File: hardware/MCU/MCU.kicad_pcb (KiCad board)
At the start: 2 copper layers, 40 x 40 mm, 39 parts, among them P1 CONN_01X05, P2 CONN_01X04, P3 CONN_01X05, U1 MAX6369, U2 DS18B20, U3 TC1262-30VDB, U4 PIC18F45K22, U5 LTC6082, Y1 Crystal

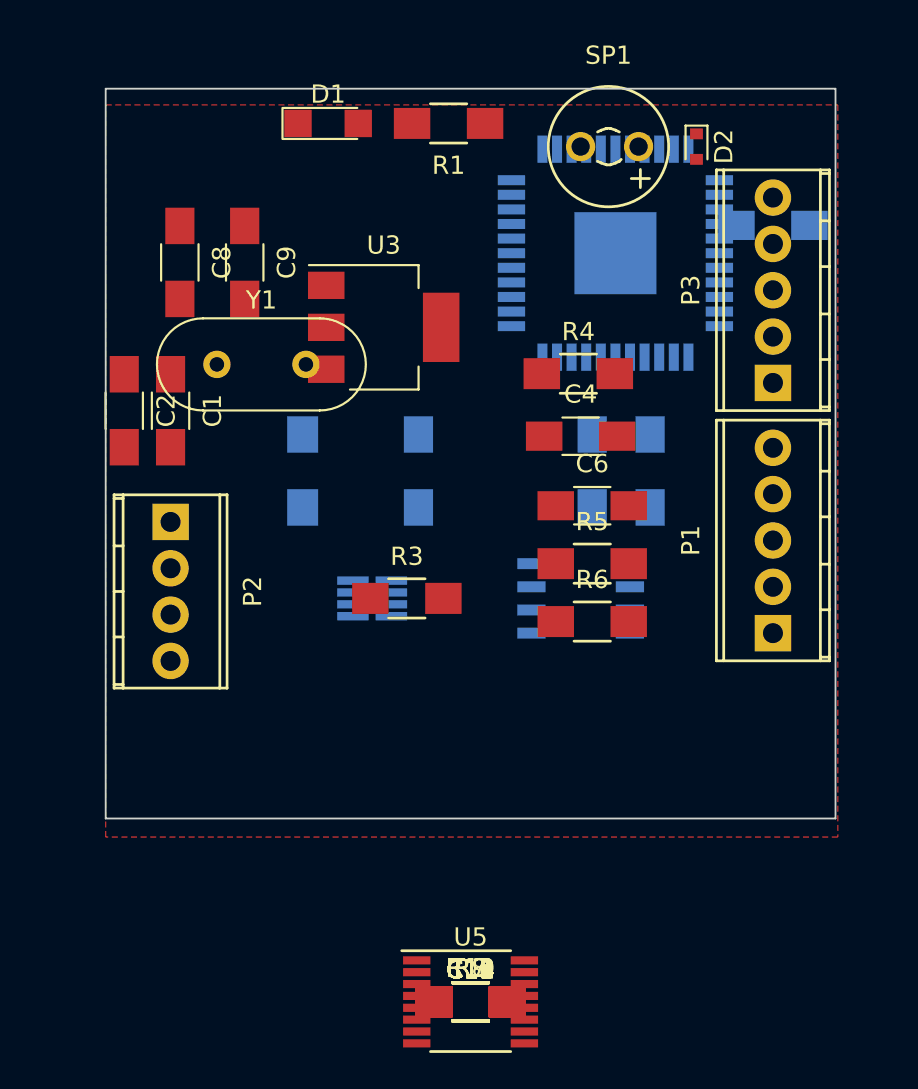
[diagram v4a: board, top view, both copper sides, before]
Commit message: Puestas todas las huellas. Primera colocacion de los componentes hecha. A la espera de la revision de los esquematicos para rutar
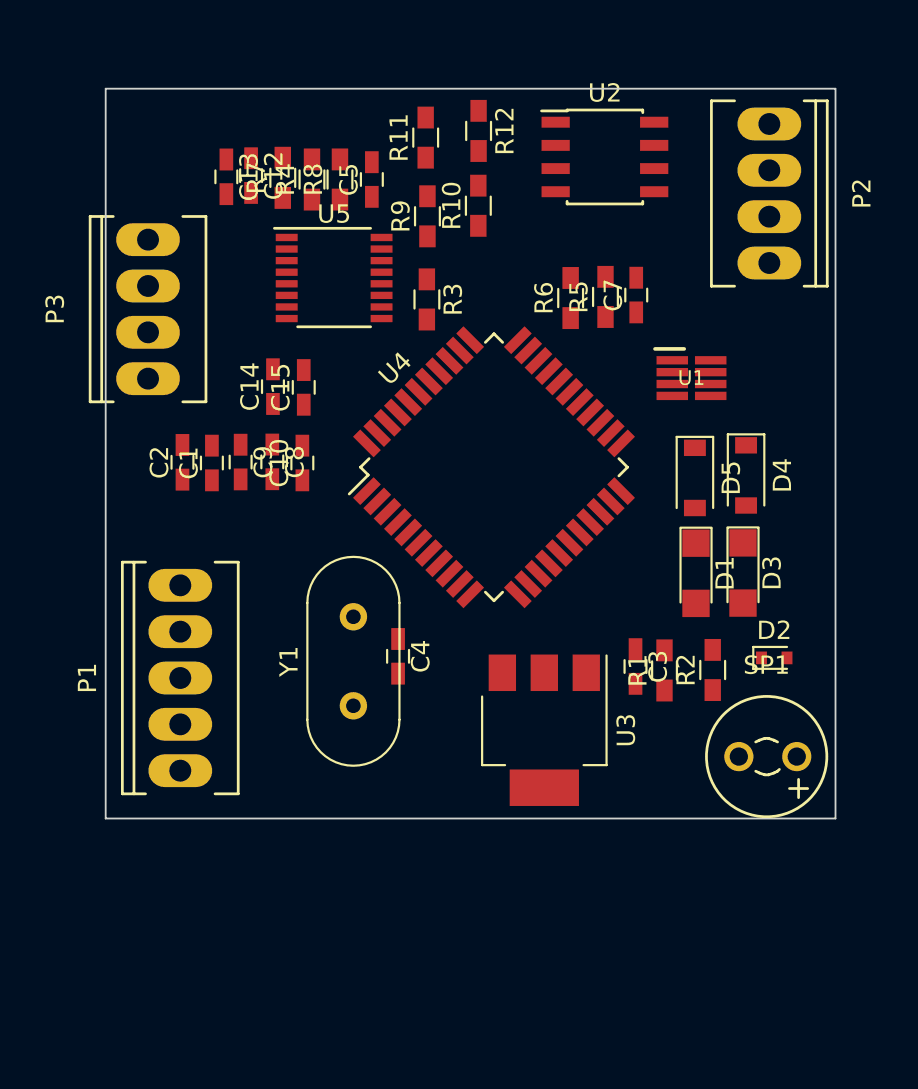
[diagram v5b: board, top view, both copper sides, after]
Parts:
- removed C11, C6: 100nF, Capacitors_SMD:C_1206_HandSoldering
- added D3: LED, LEDs:LED_1206, F.Cu at (47.0, 184.7)
- added D4: ZENER, Diodes_SMD:D_SOD-123, F.Cu at (47.2, 179.3)
- added D5: ZENER, Diodes_SMD:D_SOD-123, F.Cu at (44.4, 179.5)
- C1, C12, C13, C14, C15, C2, C4, C8, C9: footprint Capacitors_SMD:C_1206_HandSoldering -> Capacitors_SMD:C_0603_HandSoldering
- C10, C3, C5, C7: footprint Capacitors_SMD:C_1206_HandSoldering -> Capacitors_SMD:C_0603_HandSoldering; moved to F.Cu
- P1: footprint Connectors_Terminal_Blocks:TerminalBlock_Pheonix_MPT-2.54mm_5pol -> Sockets_MOLEX_KK-System:Socket_MOLEX-KK-RM2-54mm_Lock_5pin_straight
- P2: footprint Connectors_Terminal_Blocks:TerminalBlock_Pheonix_MPT-2.54mm_4pol -> Sockets_MOLEX_KK-System:Socket_MOLEX-KK-RM2-54mm_Lock_4pin_straight
- P3: footprint Connectors_Terminal_Blocks:TerminalBlock_Pheonix_MPT-2.54mm_5pol -> Sockets_MOLEX_KK-System:Socket_MOLEX-KK-RM2-54mm_Lock_4pin_straight
- R1, R10, R11, R12, R3, R4, R5, R6, R7, R8, R9: footprint Resistors_SMD:R_1206_HandSoldering -> Resistors_SMD:R_0603_HandSoldering
- R2: footprint Resistors_SMD:R_1206_HandSoldering -> Resistors_SMD:R_0603_HandSoldering; moved to F.Cu
- U1, U2: moved to F.Cu
- U4: footprint Housings_QFP:TQFP-44-1EP_10x10mm_Pitch0.8mm -> Housings_QFP:LQFP-44_10x10mm_Pitch0.8mm; moved to F.Cu
- U5: value LTC6082 -> LT6005; footprint Housings_SSOP:TSSOP-16_4.4x5mm_Pitch0.65mm -> Housings_SSOP:SSOP-16_3.9x4.9mm_Pitch0.635mm
- moved R12 47.7 mm to (32.5, 160.4), turned to 270 degrees
- moved R11 47.4 mm to (29.6, 160.8), turned to 90 degrees
- moved C13 47.2 mm to (18.7, 162.9), turned to 270 degrees
- moved C12 46.9 mm to (20.0, 162.9), turned to 270 degrees
- moved R7 46.3 mm to (21.8, 163.0), turned to 90 degrees
- moved R8 45.6 mm to (24.9, 163.1), turned to 90 degrees
- moved R10 43.6 mm to (32.5, 164.5), turned to 90 degrees
- moved R9 43.1 mm to (29.7, 165.1), turned to 90 degrees
- moved U5 40.4 mm to (24.6, 168.5)
- moved P2 37.4 mm to (48.4, 163.9)
- moved C14 35.4 mm to (21.2, 174.4), turned to 90 degrees
- moved C15 34.9 mm to (22.9, 174.5), turned to 90 degrees
- moved SP1 34.5 mm to (46.8, 194.7)
- moved P3 34.5 mm to (14.4, 170.2)
- moved P1 32.6 mm to (16.2, 190.4)
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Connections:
- C12 pad 1: Net-(C11-Pad1) -> VCC
- C12 pad 2: GND -> Net-(C12-Pad2)
- C13 pad 1: Net-(C11-Pad1) -> VCC
- C13 pad 2: GND -> Net-(C12-Pad2)
- R2 pad 2: (no net) -> Net-(D3-Pad2)
- U5 pad 12: /RF_IN -> (no net)
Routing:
- removed copper zone on F.Cu, net GND

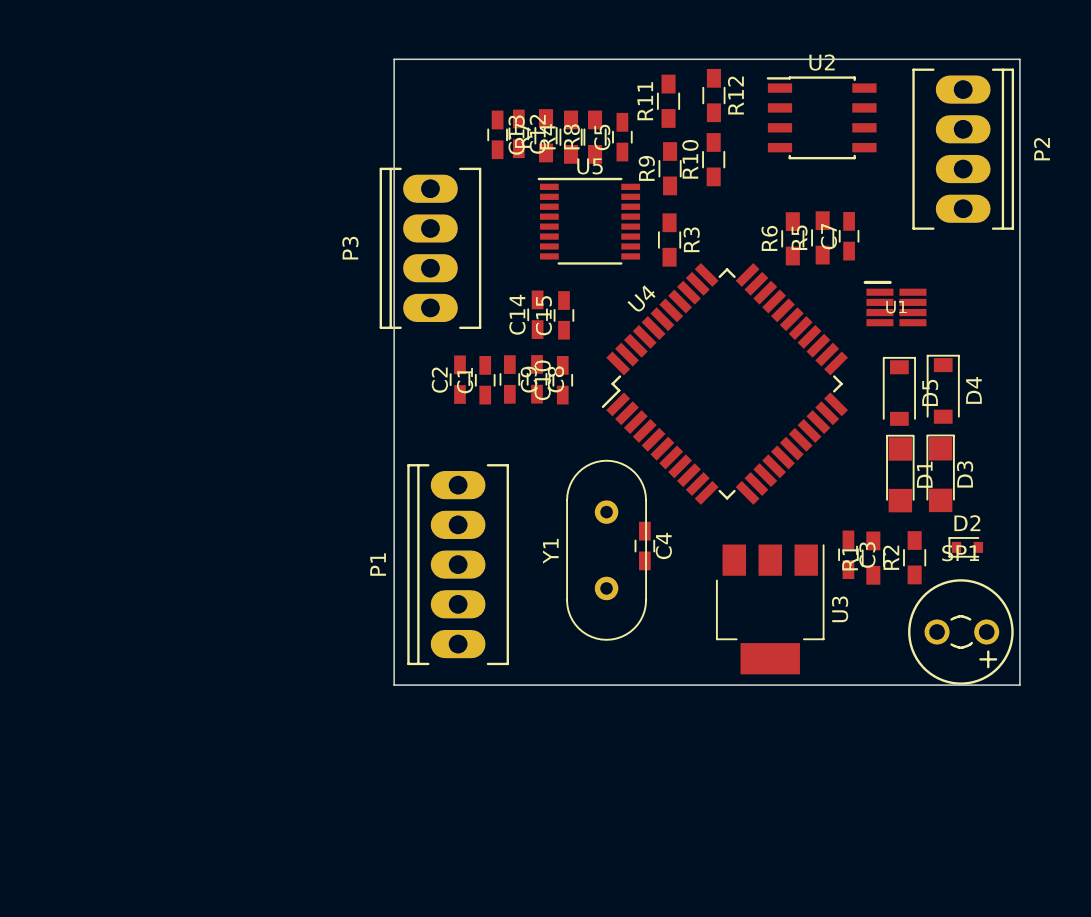
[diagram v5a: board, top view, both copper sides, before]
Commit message: Añadidas señales PTT, RPT, HIPWR, BEACON_MODE. Añadido un conector
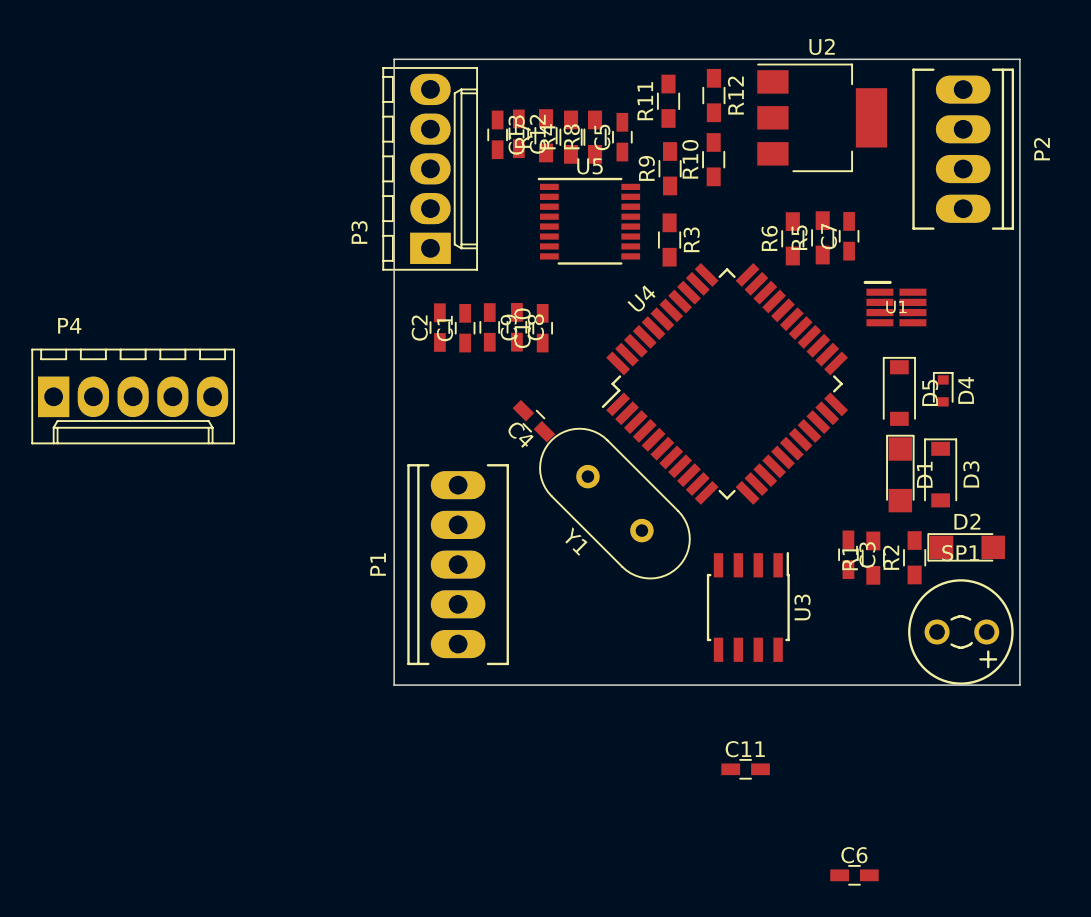
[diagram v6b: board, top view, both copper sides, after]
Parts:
- removed C14, C15: 10nF, Capacitors_SMD:C_0603_HandSoldering
- added C11: 100nF, Capacitors_SMD:C_0603_HandSoldering, F.Cu at (34.5, 203.5)
- added C6: 10nF, Capacitors_SMD:C_0603_HandSoldering, F.Cu at (41.5, 210.3)
- added P4: CONN_01X05, Connectors_Molex:Molex_KK-6410-05_05x2.54mm_Straight, F.Cu at (-9.70, 179.7)
- C1: value 18pF -> C
- C12, C13: value 100nF -> 10nF
- C4: value 1uF -> 18pF
- C5: value 10nF -> 1uF
- C7: value C -> 100nF
- D2: value D -> LED; footprint Diodes_SMD:D_SOD-523 -> LEDs:LED_1206
- D3: value LED -> ZENER; footprint LEDs:LED_1206 -> Diodes_SMD:D_SOD-123
- D4: value ZENER -> D; footprint Diodes_SMD:D_SOD-123 -> Diodes_SMD:D_SOD-523
- P3: footprint Sockets_MOLEX_KK-System:Socket_MOLEX-KK-RM2-54mm_Lock_4pin_straight -> Connectors_Molex:Molex_KK-6410-05_05x2.54mm_Straight
- U2: value DS18B20 -> TC1262-30VDB; footprint Housings_SOIC:SOIC-8_3.9x4.9mm_Pitch1.27mm -> SOT-223
- U3: value TC1262-30VDB -> DS18B20; footprint SOT-223 -> Housings_SOIC:SOIC-8_3.9x4.9mm_Pitch1.27mm
- moved C4 10.7 mm to (21.0, 181.2), turned to 135 degrees
- moved Y1 4.33 mm to (27.9, 188.2), turned to 135 degrees
- moved C9 3.57 mm to (18.2, 175.3)
- moved C2 3.57 mm to (15.0, 175.3)
- moved C10 3.57 mm to (21.6, 175.3)
- moved C8 3.57 mm to (19.9, 175.2)
- moved C1 3.57 mm to (16.6, 175.3)
- moved U3 1.41 mm to (34.7, 193.2)
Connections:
- net /BEA renamed /BEACON_ON
- net /RA0 renamed /VBAT
- C1 pad 1: /RA6 -> VCC
- C10 pad 1: /DIS -> VCC
- C10 pad 2: GND -> Net-(C10-Pad2)
- C12 pad 1: VCC -> Net-(C12-Pad1)
- C12 pad 2: Net-(C12-Pad2) -> GND
- C13 pad 1: VCC -> Net-(C13-Pad1)
- C13 pad 2: Net-(C12-Pad2) -> Net-(C13-Pad2)
- C2 pad 1: /RA7 -> /RA6
- C4 pad 1: VCC -> /RA7
- C5 pad 1: Net-(C5-Pad1) -> VCC
- C7 pad 1: VCC -> /DIS
- D2 pad 1: /BUZZER -> GND
- D2 pad 2: GND -> Net-(D2-Pad2)
- D3 pad 1: GND -> /SOL
- D3 pad 2: Net-(D3-Pad2) -> GND
- D4 pad 1: /SOL -> /BUZZER
- R1 pad 1: /LED_R -> /LED_G
- R2 pad 1: /LED_G -> /LED_R
- R2 pad 2: Net-(D3-Pad2) -> Net-(D2-Pad2)
- R4 pad 1: Net-(C5-Pad1) -> Net-(C6-Pad1)
- R7 pad 2: Net-(C15-Pad2) -> Net-(C13-Pad2)
- R8 pad 1: Net-(C15-Pad2) -> Net-(C13-Pad2)
- R8 pad 2: Net-(C14-Pad1) -> Net-(C12-Pad1)
- U1 pad 3: (no net) -> Net-(U1-Pad3)
- U2 pad 1: (no net) -> VDD
- U2 pad 2: (no net) -> GND
- U2 pad 3: (no net) -> VCC
- U2 pad 4: /TEMP -> GND
- U3 pad 1: VDD -> Net-(U3-Pad1)
- U3 pad 2: GND -> Net-(U3-Pad2)
- U3 pad 3: VCC -> Net-(U3-Pad3)
- U3 pad 4: GND -> /TEMP
- U4 pad 1: (no net) -> Net-(U4-Pad1)
- U4 pad 10: (no net) -> /RPT
- U4 pad 11: (no net) -> /HIPWR
- U4 pad 12: (no net) -> Net-(U4-Pad12)
- U4 pad 13: (no net) -> Net-(U4-Pad13)
- U4 pad 14: (no net) -> /BEACON_MODE
- U4 pad 15: (no net) -> Net-(U4-Pad15)
- U4 pad 23: (no net) -> Net-(U4-Pad23)
- U4 pad 25: (no net) -> Net-(U4-Pad25)
- U4 pad 32: (no net) -> Net-(U4-Pad32)
- U4 pad 33: (no net) -> Net-(U4-Pad33)
- U4 pad 34: (no net) -> Net-(U4-Pad34)
- U4 pad 35: (no net) -> Net-(U4-Pad35)
- U4 pad 36: (no net) -> Net-(U4-Pad36)
- U4 pad 37: (no net) -> Net-(U4-Pad37)
- U4 pad 38: (no net) -> Net-(U4-Pad38)
- U4 pad 4: (no net) -> Net-(U4-Pad4)
- U4 pad 42: (no net) -> Net-(U4-Pad42)
- U4 pad 43: (no net) -> Net-(U4-Pad43)
- U4 pad 44: (no net) -> Net-(U4-Pad44)
- U4 pad 5: (no net) -> Net-(U4-Pad5)
- U4 pad 9: (no net) -> /PTT
- U5 pad 12: (no net) -> /RF_IN
- U5 pad 3: Net-(C5-Pad1) -> Net-(C6-Pad1)
- U5 pad 5: Net-(C14-Pad1) -> Net-(C12-Pad1)
- U5 pad 6: Net-(C15-Pad1) -> Net-(C13-Pad1)

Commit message: Modificaciones para fabricación:   - Añadidos campos en los componentes (esquemáticos).   - Añadida carpeta Documentos/Montador/   - Creada primera versión del BOM (formato HTML, CSV y XML).
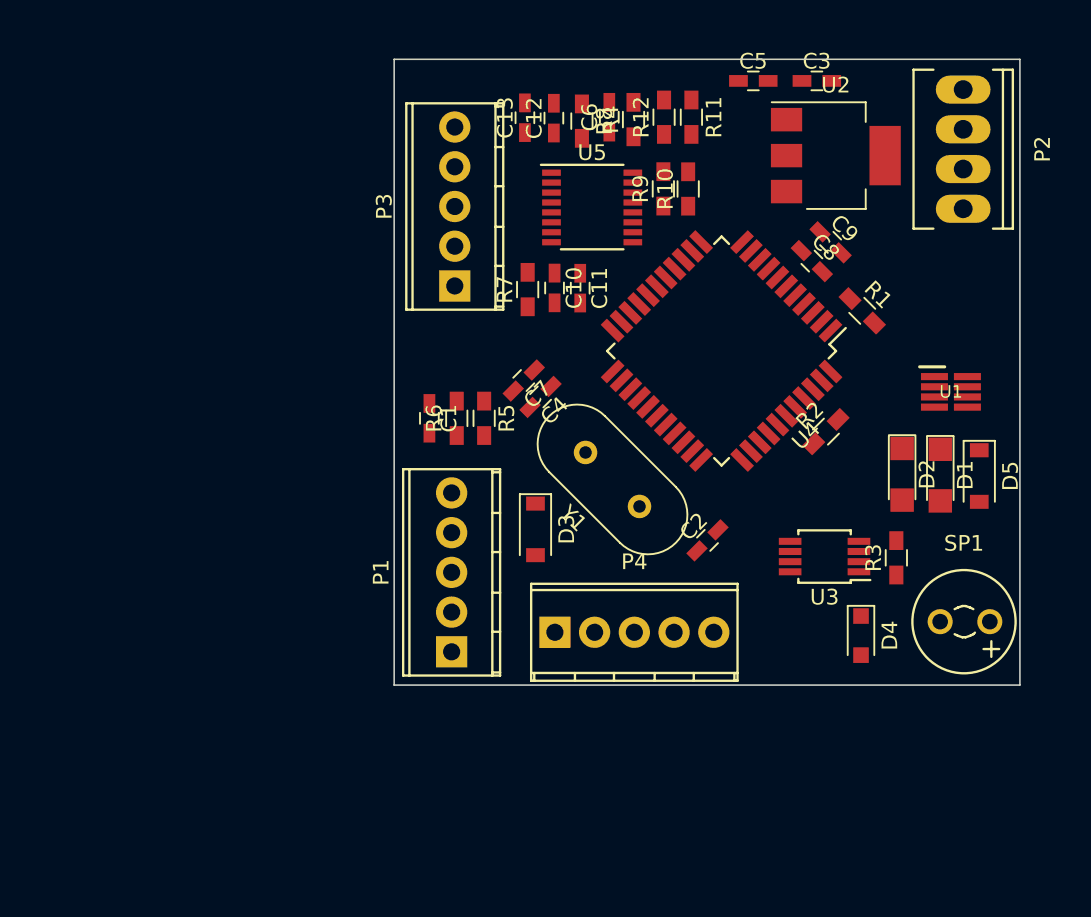
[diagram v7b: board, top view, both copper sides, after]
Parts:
- C1: value C -> 100nF
- C10: value 100nF -> 10nF
- D4: value D -> ZENER; footprint Diodes_SMD:D_SOD-523 -> Diodes_SMD:D_SOD-323_HandSoldering
- P1: footprint Sockets_MOLEX_KK-System:Socket_MOLEX-KK-RM2-54mm_Lock_5pin_straight -> Connectors_Terminal_Blocks:TerminalBlock_Pheonix_MPT-2.54mm_5pol
- P3, P4: footprint Connectors_Molex:Molex_KK-6410-05_05x2.54mm_Straight -> Connectors_Terminal_Blocks:TerminalBlock_Pheonix_MPT-2.54mm_5pol
- U3: footprint Housings_SOIC:SOIC-8_3.9x4.9mm_Pitch1.27mm -> Housings_SSOP:MSOP-8_3x3mm_Pitch0.65mm
- moved C6 50.9 mm to (25.8, 161.8), turned to 90 degrees
- moved P4 35.4 mm to (22.3, 194.7)
- moved C11 32.5 mm to (24.0, 172.7), turned to 270 degrees
- moved C3 30.4 mm to (39.1, 159.5), turned to 0 degrees
- moved D3 26.1 mm to (21.1, 188.2)
- moved R3 25.0 mm to (44.2, 190.0), turned to 90 degrees
- moved R5 24.5 mm to (17.8, 181.1), turned to 270 degrees
- moved R6 24.4 mm to (16.1, 181.1)
- moved C7 22.8 mm to (20.4, 178.7), turned to 225 degrees
- moved C9 22.5 mm to (40.0, 169.8), turned to 315 degrees
- moved C2 21.9 mm to (32.1, 188.9), turned to 45 degrees
- moved C8 19.3 mm to (38.8, 171.0), turned to 315 degrees
- moved D4 16.5 mm to (41.9, 195.0)
- moved R1 15.8 mm to (42.0, 174.2), turned to 315 degrees
- moved R7 9.90 mm to (20.6, 172.8)
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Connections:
- C10 pad 2: Net-(C10-Pad2) -> GND
- C11 pad 2: Net-(C10-Pad2) -> GND
- C12 pad 1: Net-(C12-Pad1) -> GND
- C12 pad 2: GND -> Net-(C12-Pad2)
- C8 pad 1: VCC -> VDD
- C9 pad 1: VCC -> VDD
- D2 pad 2: Net-(D2-Pad2) -> (no net)
- R2 pad 1: /LED_R -> (no net)
- R2 pad 2: Net-(D2-Pad2) -> (no net)
- R8 pad 2: Net-(C12-Pad1) -> Net-(C12-Pad2)
- U1 pad 3: Net-(U1-Pad3) -> (no net)
- U3 pad 1: Net-(U3-Pad1) -> (no net)
- U3 pad 2: Net-(U3-Pad2) -> (no net)
- U3 pad 3: Net-(U3-Pad3) -> (no net)
- U3 pad 6: Net-(U3-Pad6) -> (no net)
- U3 pad 7: Net-(U3-Pad7) -> (no net)
- U3 pad 8: Net-(U3-Pad8) -> (no net)
- U4 pad 1: Net-(U4-Pad1) -> (no net)
- U4 pad 12: Net-(U4-Pad12) -> (no net)
- U4 pad 13: Net-(U4-Pad13) -> (no net)
- U4 pad 15: Net-(U4-Pad15) -> (no net)
- U4 pad 23: Net-(U4-Pad23) -> (no net)
- U4 pad 25: Net-(U4-Pad25) -> (no net)
- U4 pad 32: Net-(U4-Pad32) -> (no net)
- U4 pad 33: Net-(U4-Pad33) -> (no net)
- U4 pad 34: Net-(U4-Pad34) -> (no net)
- U4 pad 35: Net-(U4-Pad35) -> (no net)
- U4 pad 36: Net-(U4-Pad36) -> (no net)
- U4 pad 37: Net-(U4-Pad37) -> (no net)
- U4 pad 38: Net-(U4-Pad38) -> (no net)
- U4 pad 39: /LED_R -> (no net)
- U4 pad 4: Net-(U4-Pad4) -> (no net)
- U4 pad 42: Net-(U4-Pad42) -> (no net)
- U4 pad 43: Net-(U4-Pad43) -> (no net)
- U4 pad 44: Net-(U4-Pad44) -> (no net)
- U4 pad 5: Net-(U4-Pad5) -> (no net)
- U5 pad 5: Net-(C12-Pad1) -> Net-(C12-Pad2)
